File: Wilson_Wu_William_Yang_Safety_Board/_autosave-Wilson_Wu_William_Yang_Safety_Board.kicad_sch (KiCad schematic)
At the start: 33 parts, among them J1 22035035, J2 XT60-M, J3 XT60-M, J4 M22-7130442, J5 Molex Micro-Fit 4 Pin, J6 430450200, J7 430450200, Q1 IRLML6344TRPBF, U2 MCP2562-E/P, U3 MCP6286T-E/OT, U4 4002, U5 100 ohm, U6 J115F11A12VDCS6.9, U7 LM1117IDTX-3.3/NOPB

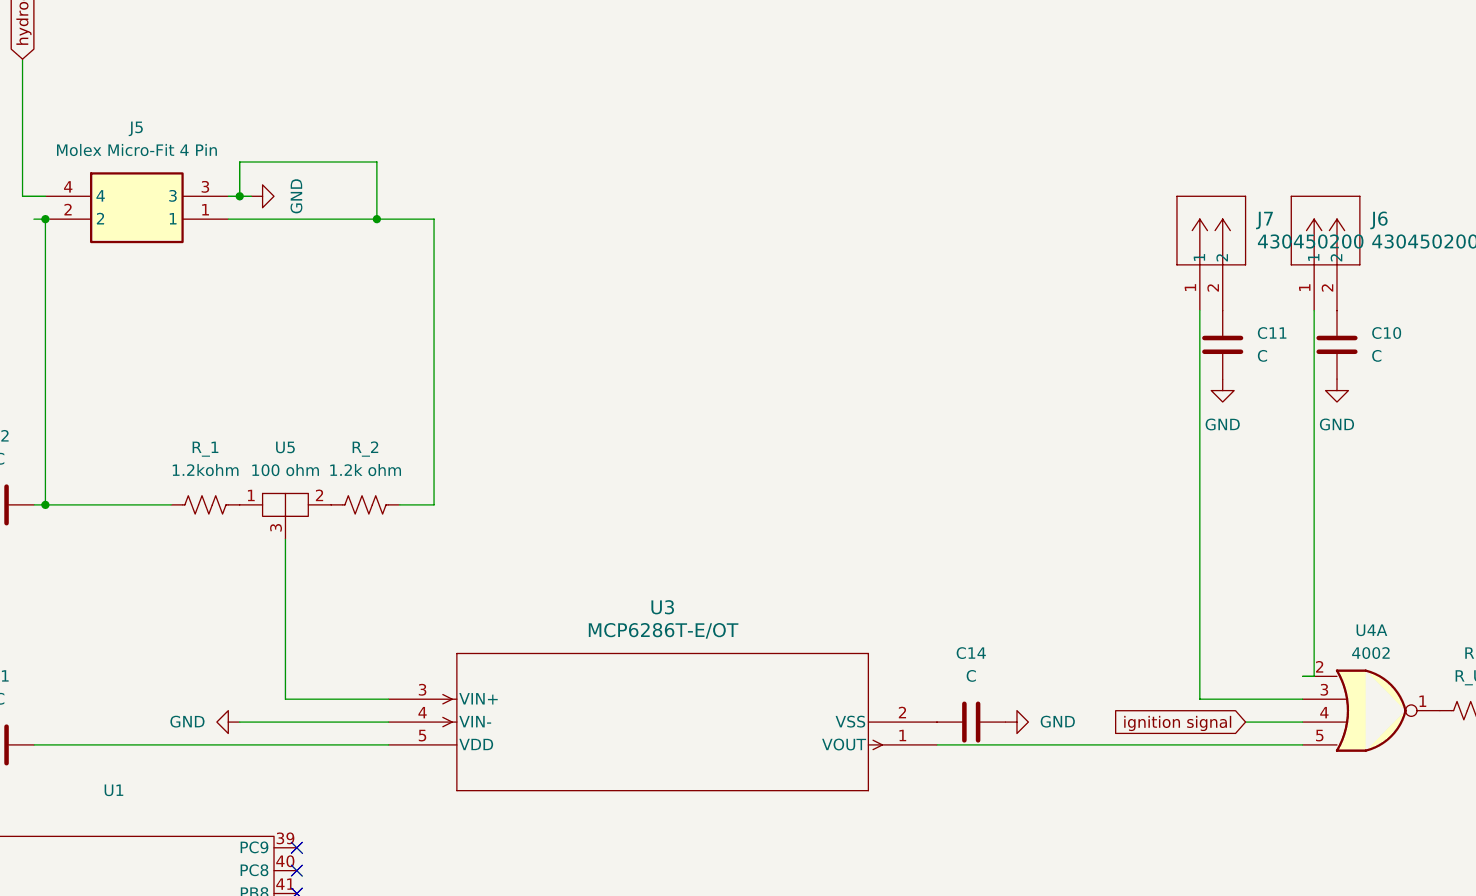
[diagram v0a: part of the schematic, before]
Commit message: added new nor gate
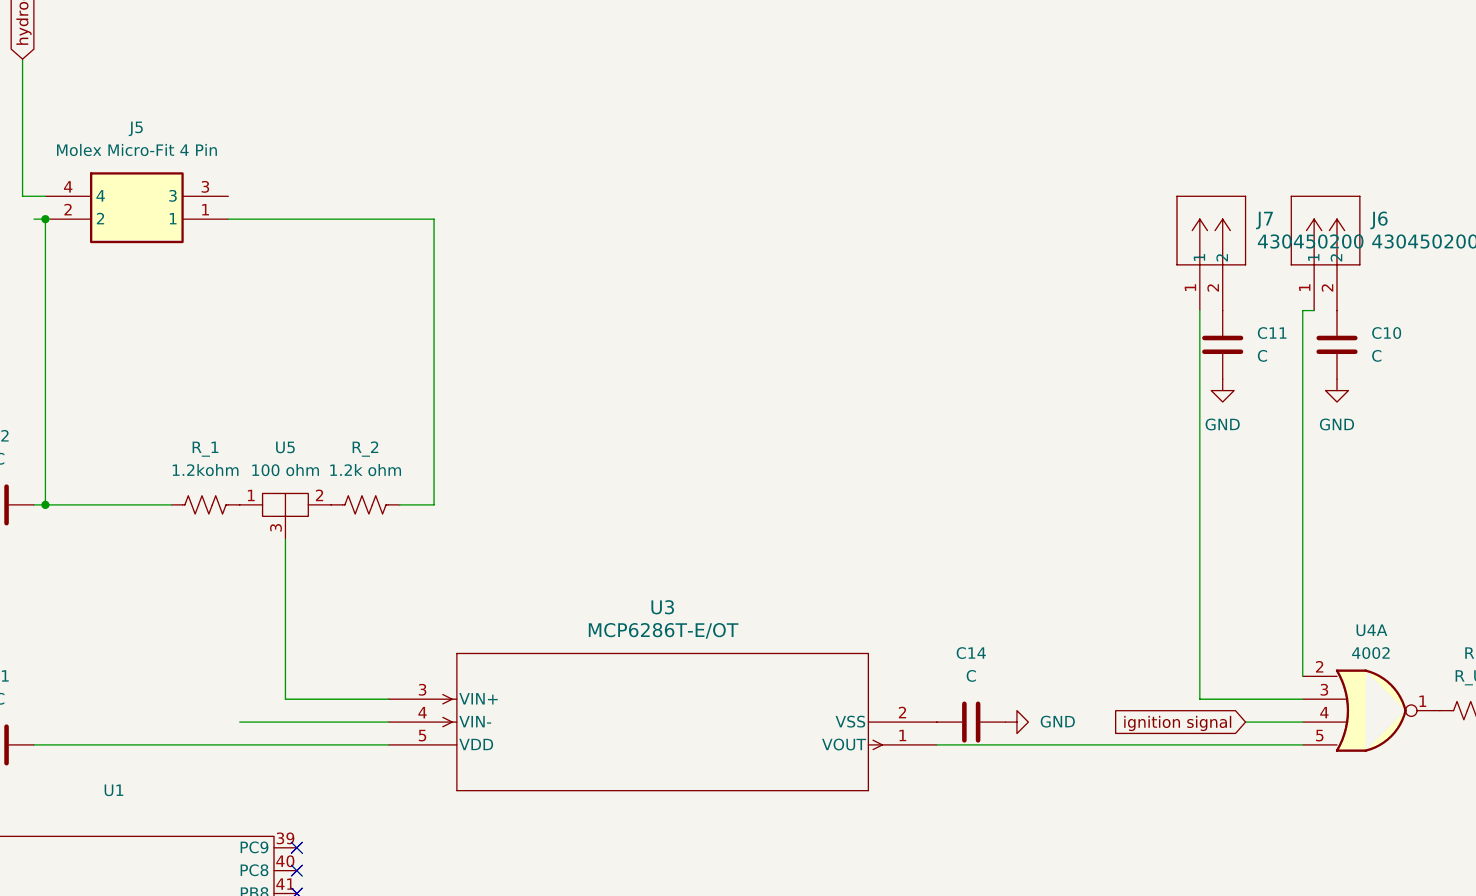
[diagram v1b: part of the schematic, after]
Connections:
- net GND: no longer J5.1, J5.3, R_2.2, U3.4 (VIN-)
- new net: J5.1, R_2.2
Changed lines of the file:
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@@
 	(paper "A4")
 	(junction
-		(at 71.12 22.86)
-		(diameter 0)
-		(color 0 0 0 0)
-	)
-	(junction
 		(at 220.98 54.61)
 		(diameter 0)
@@
 	)
 	(junction
-		(at 86.36 25.4)
-		(diameter 0)
-		(color 0 0 0 0)
-	)
-	(junction
 		(at 49.53 57.15)
 		(diameter 0)
@@
 	(wire
 		(pts
-			(xy 190.5 76.2) (xy 190.5 35.56)
+			(xy 189.23 76.2) (xy 189.23 35.56)
 		)
 		(stroke
@@
 	(wire
 		(pts
-			(xy 48.26 25.4) (xy 49.53 25.4)
+			(xy 189.23 35.56) (xy 190.5 35.56)
 		)
 		(stroke
@@
 	(wire
 		(pts
-			(xy 71.12 22.86) (xy 72.39 22.86)
+			(xy 48.26 25.4) (xy 49.53 25.4)
 		)
 		(stroke
@@
 	(wire
 		(pts
-			(xy 71.12 19.05) (xy 71.12 22.86)
-		)
-		(stroke
-			(width 0)
-			(type default)
-		)
-	)
-	(wire
-		(pts
-			(xy 69.85 22.86) (xy 71.12 22.86)
-		)
-		(stroke
-			(width 0)
-			(type default)
-		)
-	)
-	(wire
-		(pts
 			(xy 148.59 83.82) (xy 189.23 83.82)
 		)
@@
 	(wire
 		(pts
-			(xy 86.36 25.4) (xy 86.36 19.05)
-		)
-		(stroke
-			(width 0)
-			(type default)
-		)
-	)
-	(wire
-		(pts
 			(xy 260.35 132.08) (xy 251.46 132.08)
 		)
@@
 	(wire
 		(pts
-			(xy 69.85 25.4) (xy 86.36 25.4)
+			(xy 69.85 25.4) (xy 92.71 25.4)
 		)
 		(stroke
@@
 	(wire
 		(pts
-			(xy 92.71 25.4) (xy 86.36 25.4)
-		)
-		(stroke
-			(width 0)
-			(type default)
-		)
-	)
-	(wire
-		(pts
 			(xy 76.2 60.96) (xy 76.2 78.74)
 		)
@@
 	(wire
 		(pts
-			(xy 189.23 76.2) (xy 190.5 76.2)
-		)
-		(stroke
-			(width 0)
-			(type default)
-		)
-	)
-	(wire
-		(pts
 			(xy 275.59 55.88) (xy 270.51 55.88)
 		)
@@
 	(wire
 		(pts
-			(xy 86.36 19.05) (xy 71.12 19.05)
-		)
-		(stroke
-			(width 0)
-			(type default)
-		)
-	)
-	(wire
-		(pts
 			(xy 217.17 25.4) (xy 217.17 27.94)
 		)
@@
 	(symbol
 		(lib_id "power:GND")
-		(at 71.12 81.28 270)
-		(unit 1)
-		(exclude_from_sim no)
-		(in_bom yes)
-		(on_board yes)
-		(dnp no)
-		(fields_autoplaced yes)
-		(property "Reference" "#PWR019"
-			(at 64.77 81.28 0)
-			(effects
-				(font
-					(size 1.27 1.27)
-				)
-				(hide yes)
-			)
-		)
-		(property "Value" "GND"
-			(at 67.31 81.2799 90)
-			(effects
-				(font
-					(size 1.27 1.27)
-				)
-				(justify right)
-			)
-		)
-		(property "Footprint" ""
-			(at 71.12 81.28 0)
-			(effects
-				(font
-					(size 1.27 1.27)
-				)
-				(hide yes)
-			)
-		)
-		(property "Datasheet" ""
-			(at 71.12 81.28 0)
-			(effects
-				(font
-					(size 1.27 1.27)
-				)
-				(hide yes)
-			)
-		)
-		(property "Description" "Power symbol creates a global label with name \"GND\" , ground"
-			(at 71.12 81.28 0)
-			(effects
-				(font
-					(size 1.27 1.27)
-				)
-				(hide yes)
-			)
-		)
-		(pin "1"
-		)
-		(instances
-			(project ""
-				(path "/fa857c32-0741-4b91-b122-1a57686bb514"
-					(reference "#PWR019")
-					(unit 1)
-				)
-			)
-		)
-	)
-	(symbol
-		(lib_id "power:GND")
 		(at 273.05 25.4 0)
 		(unit 1)
@@
 					(unit 1)
 				)
-			)
-		)
-	)
-	(symbol
-		(lib_id "power:GND")
-		(at 72.39 22.86 90)
-		(unit 1)
-		(exclude_from_sim no)
-		(in_bom yes)
-		(on_board yes)
-		(dnp no)
-		(fields_autoplaced yes)
-		(property "Reference" "#PWR010"
-			(at 78.74 22.86 0)
-			(effects
-				(font
-					(size 1.27 1.27)
-				)
-				(hide yes)
-			)
-		)
-		(property "Value" "GND"
-			(at 77.47 22.86 0)
-			(effects
-				(font
-					(size 1.27 1.27)
-				)
-			)
-		)
-		(property "Footprint" ""
-			(at 72.39 22.86 0)
-			(effects
-				(font
-					(size 1.27 1.27)
-				)
-				(hide yes)
-			)
-		)
-		(property "Datasheet" ""
-			(at 72.39 22.86 0)
-			(effects
-				(font
-					(size 1.27 1.27)
-				)
-				(hide yes)
-			)
-		)
-		(property "Description" "Power symbol creates a global label with name \"GND\" , ground"
-			(at 72.39 22.86 0)
-			(effects
-				(font
-					(size 1.27 1.27)
-				)
-				(hide yes)
-			)
-		)
-		(pin "1"
-		)
-		(instances
-			(project ""
-				(path "/fa857c32-0741-4b91-b122-1a57686bb514"
-					(reference "#PWR010")
-					(unit 1)
-				)
